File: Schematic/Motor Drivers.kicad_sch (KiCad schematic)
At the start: 16 parts, among them U18 DRV8243SQDGQRQ1 (S-Variant), U19 DRV8243SQDGQRQ1 (S-Variant)

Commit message: 100n cap
100n cap bom
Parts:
- C71, C72: footprint (none) -> CL10B104MB8NNNC:CAPC1608X90N; Link (none) -> https://mou.sr/3JWJm45; Manufacturer Part Number (none) -> CL10B104MB8NNNC; Price per Unit (none) -> 0.10; Supplier (none) -> Mouser; Supplier Part Number (none) -> 187-CL10B104MB8NNNC
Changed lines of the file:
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@@
 			)
 		)
-		(property "Footprint" ""
+		(property "Footprint" "CL10B104MB8NNNC:CAPC1608X90N"
 			(at 69.5452 59.69 0)
 			(effects
@@
 			)
 		)
-		(property "Link" ""
+		(property "Link" "https://mou.sr/3JWJm45"
 			(at 68.58 55.88 0)
 			(effects
@@
 			)
 		)
-		(property "Manufacturer Part Number" ""
+		(property "Manufacturer Part Number" "CL10B104MB8NNNC"
 			(at 68.58 55.88 0)
 			(effects
@@
 			)
 		)
-		(property "Price per Unit" ""
+		(property "Price per Unit" "0.10"
 			(at 68.58 55.88 0)
 			(effects
@@
 			)
 		)
-		(property "Supplier" ""
+		(property "Supplier" "Mouser"
 			(at 68.58 55.88 0)
 			(effects
@@
 			)
 		)
-		(property "Supplier Part Number" ""
+		(property "Supplier Part Number" "187-CL10B104MB8NNNC "
 			(at 68.58 55.88 0)
 			(effects
@@
 			)
 		)
-		(property "Footprint" ""
+		(property "Footprint" "CL10B104MB8NNNC:CAPC1608X90N"
 			(at 67.0052 128.27 0)
 			(effects
@@
 			)
 		)
-		(property "Link" ""
+		(property "Link" "https://mou.sr/3JWJm45"
 			(at 66.04 124.46 0)
 			(effects
@@
 			)
 		)
-		(property "Manufacturer Part Number" ""
+		(property "Manufacturer Part Number" "CL10B104MB8NNNC"
 			(at 66.04 124.46 0)
 			(effects
@@
 			)
 		)
-		(property "Price per Unit" ""
+		(property "Price per Unit" "0.10"
 			(at 66.04 124.46 0)
 			(effects
@@
 			)
 		)
-		(property "Supplier" ""
+		(property "Supplier" "Mouser"
 			(at 66.04 124.46 0)
 			(effects
@@
 			)
 		)
-		(property "Supplier Part Number" ""
+		(property "Supplier Part Number" "187-CL10B104MB8NNNC "
 			(at 66.04 124.46 0)
 			(effects

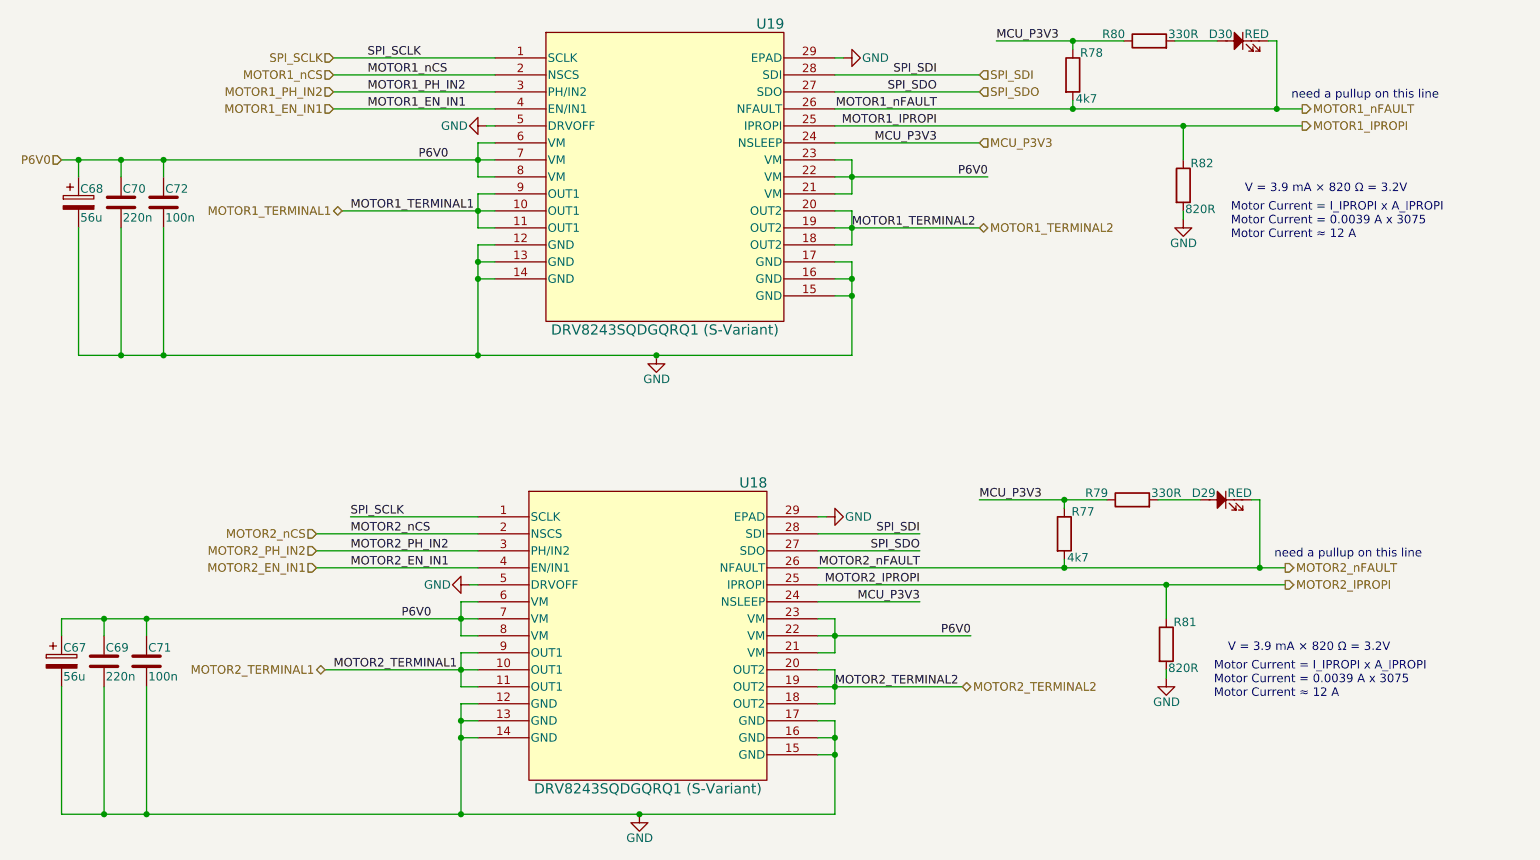
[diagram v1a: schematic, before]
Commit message: added test points and fet
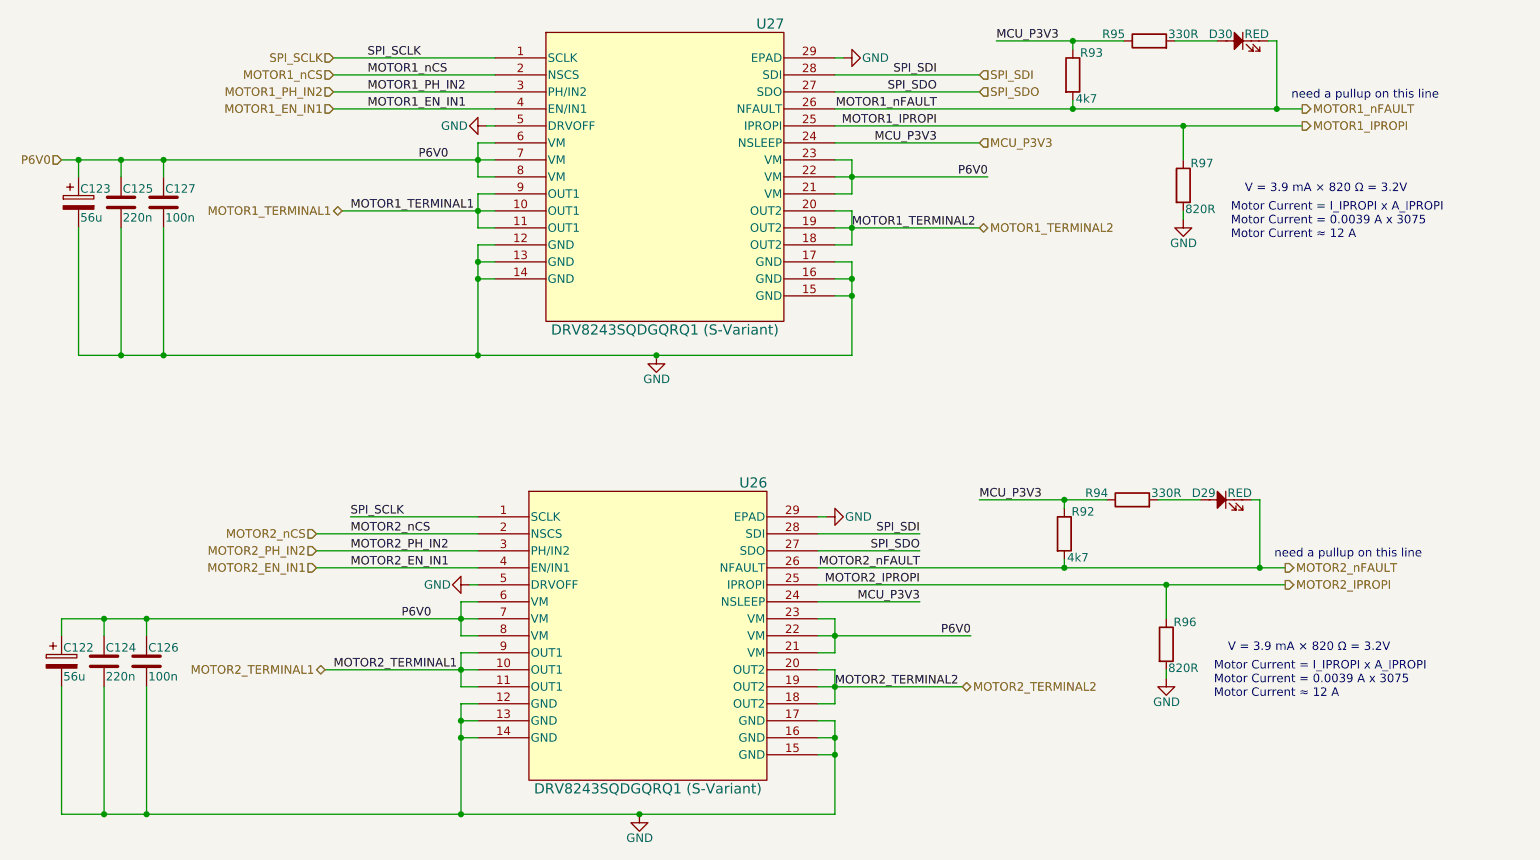
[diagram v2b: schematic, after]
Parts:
- C126: renamed from C71; footprint CL10B104MB8NNNC:CAPC1608X90N -> Capacitor_SMD:C_0603_1608Metric_Pad1.08x0.95mm_HandSolder
- C127: renamed from C72; footprint CL10B104MB8NNNC:CAPC1608X90N -> Capacitor_SMD:C_0603_1608Metric_Pad1.08x0.95mm_HandSolder
- renumbered C67 to C122, C68 to C123, C69 to C124, C70 to C125, R77 to R92, R78 to R93, R79 to R94, R80 to R95, R81 to R96, R82 to R97, U18 to U26, U19 to U27
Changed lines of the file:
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@@
 		(on_board yes)
 		(dnp no)
-		(property "Reference" "C72"
+		(property "Reference" "C127"
 			(at 68.834 53.848 0)
 			(effects
@@
 			)
 		)
-		(property "Footprint" "CL10B104MB8NNNC:CAPC1608X90N"
+		(property "Footprint" "Capacitor_SMD:C_0603_1608Metric_Pad1.08x0.95mm_HandSolder"
 			(at 69.5452 59.69 0)
 			(effects
@@
 			(project "STAR"
 				(path "/fc8533bc-25dd-4c20-9b4c-ffebebd6739b/f73d6367-f3ba-42df-a3ea-bd155f1c219f/07712c52-f5ae-4a00-8c08-8de30640eab9"
-					(reference "C72")
+					(reference "C127")
 					(unit 1)
 				)
@@
 		(on_board yes)
 		(dnp no)
-		(property "Reference" "R79"
+		(property "Reference" "R94"
 			(at 208.026 99.314 90)
 			(effects
@@
 			(project "STAR"
 				(path "/fc8533bc-25dd-4c20-9b4c-ffebebd6739b/f73d6367-f3ba-42df-a3ea-bd155f1c219f/07712c52-f5ae-4a00-8c08-8de30640eab9"
-					(reference "R79")
+					(reference "R94")
 					(unit 1)
 				)
@@
 		(on_board yes)
 		(dnp no)
-		(property "Reference" "#PWR043"
+		(property "Reference" "#PWR068"
 			(at 110.49 44.45 0)
 			(effects
@@
 			(project "STAR"
 				(path "/fc8533bc-25dd-4c20-9b4c-ffebebd6739b/f73d6367-f3ba-42df-a3ea-bd155f1c219f/07712c52-f5ae-4a00-8c08-8de30640eab9"
-					(reference "#PWR043")
+					(reference "#PWR068")
 					(unit 1)
 				)
@@
 		(on_board yes)
 		(dnp no)
-		(property "Reference" "#PWR046"
+		(property "Reference" "#PWR071"
 			(at 173.99 102.87 0)
 			(effects
@@
 			(project "STAR"
 				(path "/fc8533bc-25dd-4c20-9b4c-ffebebd6739b/f73d6367-f3ba-42df-a3ea-bd155f1c219f/07712c52-f5ae-4a00-8c08-8de30640eab9"
-					(reference "#PWR046")
+					(reference "#PWR071")
 					(unit 1)
 				)
@@
 		(on_board yes)
 		(dnp no)
-		(property "Reference" "R80"
+		(property "Reference" "R95"
 			(at 210.566 30.734 90)
 			(effects
@@
 			(project "STAR"
 				(path "/fc8533bc-25dd-4c20-9b4c-ffebebd6739b/f73d6367-f3ba-42df-a3ea-bd155f1c219f/07712c52-f5ae-4a00-8c08-8de30640eab9"
-					(reference "R80")
+					(reference "R95")
 					(unit 1)
 				)
@@
 		(on_board yes)
 		(dnp no)
-		(property "Reference" "#PWR047"
+		(property "Reference" "#PWR072"
 			(at 176.53 34.29 0)
 			(effects
@@
 			(project "STAR"
 				(path "/fc8533bc-25dd-4c20-9b4c-ffebebd6739b/f73d6367-f3ba-42df-a3ea-bd155f1c219f/07712c52-f5ae-4a00-8c08-8de30640eab9"
-					(reference "#PWR047")
+					(reference "#PWR072")
 					(unit 1)
 				)
@@
 		(on_board yes)
 		(dnp no)
-		(property "Reference" "C70"
+		(property "Reference" "C125"
 			(at 62.484 53.848 0)
 			(effects
@@
 			(project "STAR"
 				(path "/fc8533bc-25dd-4c20-9b4c-ffebebd6739b/f73d6367-f3ba-42df-a3ea-bd155f1c219f/07712c52-f5ae-4a00-8c08-8de30640eab9"
-					(reference "C70")
+					(reference "C125")
 					(unit 1)
 				)
@@
 		(on_board yes)
 		(dnp no)
-		(property "Reference" "C68"
+		(property "Reference" "C123"
 			(at 56.134 53.848 0)
 			(effects
@@
 			(project "STAR"
 				(path "/fc8533bc-25dd-4c20-9b4c-ffebebd6739b/f73d6367-f3ba-42df-a3ea-bd155f1c219f/07712c52-f5ae-4a00-8c08-8de30640eab9"
-					(reference "C68")
+					(reference "C123")
 					(unit 1)
 				)
@@
 		(on_board yes)
 		(dnp no)
-		(property "Reference" "U19"
+		(property "Reference" "U27"
 			(at 159.258 29.21 0)
 			(effects
@@
 			(project "STAR"
 				(path "/fc8533bc-25dd-4c20-9b4c-ffebebd6739b/f73d6367-f3ba-42df-a3ea-bd155f1c219f/07712c52-f5ae-4a00-8c08-8de30640eab9"
-					(reference "U19")
+					(reference "U27")
 					(unit 1)
 				)
@@
 		(on_board yes)
 		(dnp no)
-		(property "Reference" "C67"
+		(property "Reference" "C122"
 			(at 53.594 122.428 0)
 			(effects
@@
 			(project "STAR"
 				(path "/fc8533bc-25dd-4c20-9b4c-ffebebd6739b/f73d6367-f3ba-42df-a3ea-bd155f1c219f/07712c52-f5ae-4a00-8c08-8de30640eab9"
-					(reference "C67")
+					(reference "C122")
 					(unit 1)
 				)
@@
 		(on_board yes)
 		(dnp no)
-		(property "Reference" "U18"
+		(property "Reference" "U26"
 			(at 156.718 97.79 0)
 			(effects
@@
 			(project "STAR"
 				(path "/fc8533bc-25dd-4c20-9b4c-ffebebd6739b/f73d6367-f3ba-42df-a3ea-bd155f1c219f/07712c52-f5ae-4a00-8c08-8de30640eab9"
-					(reference "U18")
+					(reference "U26")
 					(unit 1)
 				)
@@
 		(on_board yes)
 		(dnp no)
-		(property "Reference" "R82"
+		(property "Reference" "R97"
 			(at 223.774 50.038 0)
 			(effects
@@
 			(project "STAR"
 				(path "/fc8533bc-25dd-4c20-9b4c-ffebebd6739b/f73d6367-f3ba-42df-a3ea-bd155f1c219f/07712c52-f5ae-4a00-8c08-8de30640eab9"
-					(reference "R82")
+					(reference "R97")
 					(unit 1)
 				)
@@
 		(on_board yes)
 		(dnp no)
-		(property "Reference" "R77"
+		(property "Reference" "R92"
 			(at 205.994 102.108 0)
 			(effects
@@
 			(project "STAR"
 				(path "/fc8533bc-25dd-4c20-9b4c-ffebebd6739b/f73d6367-f3ba-42df-a3ea-bd155f1c219f/07712c52-f5ae-4a00-8c08-8de30640eab9"
-					(reference "R77")
+					(reference "R92")
 					(unit 1)
 				)
@@
 		(on_board yes)
 		(dnp no)
-		(property "Reference" "#PWR044"
+		(property "Reference" "#PWR069"
 			(at 139.7 153.67 0)
 			(effects
@@
 			(project "STAR"
 				(path "/fc8533bc-25dd-4c20-9b4c-ffebebd6739b/f73d6367-f3ba-42df-a3ea-bd155f1c219f/07712c52-f5ae-4a00-8c08-8de30640eab9"
-					(reference "#PWR044")
+					(reference "#PWR069")
 					(unit 1)
 				)
@@
 		(on_board yes)
 		(dnp no)
-		(property "Reference" "C71"
+		(property "Reference" "C126"
 			(at 66.294 122.428 0)
 			(effects
@@
 			)
 		)
-		(property "Footprint" "CL10B104MB8NNNC:CAPC1608X90N"
+		(property "Footprint" "Capacitor_SMD:C_0603_1608Metric_Pad1.08x0.95mm_HandSolder"
 			(at 67.0052 128.27 0)
 			(effects
@@
 			(project "STAR"
 				(path "/fc8533bc-25dd-4c20-9b4c-ffebebd6739b/f73d6367-f3ba-42df-a3ea-bd155f1c219f/07712c52-f5ae-4a00-8c08-8de30640eab9"
-					(reference "C71")
+					(reference "C126")
 					(unit 1)
 				)
@@
 		(on_board yes)
 		(dnp no)
-		(property "Reference" "#PWR049"
+		(property "Reference" "#PWR074"
 			(at 220.98 64.77 0)
 			(effects
@@
 			(project "STAR"
 				(path "/fc8533bc-25dd-4c20-9b4c-ffebebd6739b/f73d6367-f3ba-42df-a3ea-bd155f1c219f/07712c52-f5ae-4a00-8c08-8de30640eab9"
-					(reference "#PWR049")
+					(reference "#PWR074")
 					(unit 1)
 				)
@@
 		(on_board yes)
 		(dnp no)
-		(property "Reference" "#PWR042"
+		(property "Reference" "#PWR067"
 			(at 107.95 113.03 0)
 			(effects
@@
 			(project "STAR"
 				(path "/fc8533bc-25dd-4c20-9b4c-ffebebd6739b/f73d6367-f3ba-42df-a3ea-bd155f1c219f/07712c52-f5ae-4a00-8c08-8de30640eab9"
-					(reference "#PWR042")
+					(reference "#PWR067")
 					(unit 1)
 				)
@@
 		(on_board yes)
 		(dnp no)
-		(property "Reference" "C69"
+		(property "Reference" "C124"
 			(at 59.944 122.428 0)
 			(effects
@@
 			(project "STAR"
 				(path "/fc8533bc-25dd-4c20-9b4c-ffebebd6739b/f73d6367-f3ba-42df-a3ea-bd155f1c219f/07712c52-f5ae-4a00-8c08-8de30640eab9"
-					(reference "C69")
+					(reference "C124")
 					(unit 1)
 				)
@@
 		(on_board yes)
 		(dnp no)
-		(property "Reference" "#PWR048"
+		(property "Reference" "#PWR073"
 			(at 218.44 133.35 0)
 			(effects
@@
 			(project "STAR"
 				(path "/fc8533bc-25dd-4c20-9b4c-ffebebd6739b/f73d6367-f3ba-42df-a3ea-bd155f1c219f/07712c52-f5ae-4a00-8c08-8de30640eab9"
-					(reference "#PWR048")
+					(reference "#PWR073")
 					(unit 1)
 				)
@@
 		(on_board yes)
 		(dnp no)
-		(property "Reference" "R81"
+		(property "Reference" "R96"
 			(at 221.234 118.618 0)
 			(effects
@@
 			(project "STAR"
 				(path "/fc8533bc-25dd-4c20-9b4c-ffebebd6739b/f73d6367-f3ba-42df-a3ea-bd155f1c219f/07712c52-f5ae-4a00-8c08-8de30640eab9"
-					(reference "R81")
+					(reference "R96")
 					(unit 1)
 				)
@@
 		(on_board yes)
 		(dnp no)
-		(property "Reference" "R78"
+		(property "Reference" "R93"
 			(at 207.264 33.528 0)
 			(effects
@@
 			(project "STAR"
 				(path "/fc8533bc-25dd-4c20-9b4c-ffebebd6739b/f73d6367-f3ba-42df-a3ea-bd155f1c219f/07712c52-f5ae-4a00-8c08-8de30640eab9"
-					(reference "R78")
+					(reference "R93")
 					(unit 1)
 				)
@@
 		(on_board yes)
 		(dnp no)
-		(property "Reference" "#PWR045"
+		(property "Reference" "#PWR070"
 			(at 142.24 85.09 0)
 			(effects
@@
 			(project "STAR"
 				(path "/fc8533bc-25dd-4c20-9b4c-ffebebd6739b/f73d6367-f3ba-42df-a3ea-bd155f1c219f/07712c52-f5ae-4a00-8c08-8de30640eab9"
-					(reference "#PWR045")
+					(reference "#PWR070")
 					(unit 1)
 				)

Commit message: More REsistor
16 res down for bom
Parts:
- R92, R93: footprint (none) -> Resistor_SMD:R_0603_1608Metric_Pad0.98x0.95mm_HandSolder; Link (none) -> https://mou.sr/48a41vp; Manufacturer Part Number (none) -> RCS06034K70FKEA; Price per Unit (none) -> 0.13; Supplier (none) -> Mouser; Supplier Part Number (none) -> 71-RCS06034K70FKEA
- R95: footprint (none) -> Resistor_SMD:R_0603_1608Metric_Pad0.98x0.95mm_HandSolder; Link (none) -> https://mou.sr/4m95jdp; Manufacturer Part Number (none) -> RG1608P-331-D-T5; Price per Unit (none) -> 0.10; Supplier (none) -> Mouser; Supplier Part Number (none) -> 754-RG1608P-331DT5
- R96: footprint (none) -> Resistor_SMD:R_0603_1608Metric_Pad0.98x0.95mm_HandSolder; Link (none) -> https://mou.sr/46iPyuQ; Manufacturer Part Number (none) -> RMC1/16K8200FTP; Price per Unit (none) -> 0.10; Supplier (none) -> Mouser; Supplier Part Number (none) -> 791-RMC1/16K8200FTP
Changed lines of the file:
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@@
 			)
 		)
-		(property "Footprint" ""
+		(property "Footprint" "Resistor_SMD:R_0603_1608Metric_Pad0.98x0.95mm_HandSolder"
 			(at 215.9 33.528 90)
 			(effects
@@
 			)
 		)
-		(property "Link" ""
+		(property "Link" "https://mou.sr/4m95jdp"
 			(at 215.9 31.75 90)
 			(effects
@@
 			)
 		)
-		(property "Manufacturer Part Number" ""
+		(property "Manufacturer Part Number" "RG1608P-331-D-T5 "
 			(at 215.9 31.75 90)
 			(effects
@@
 			)
 		)
-		(property "Price per Unit" ""
+		(property "Price per Unit" "0.10"
 			(at 215.9 31.75 90)
 			(effects
@@
 			)
 		)
+		(property "Supplier" "Mouser"
+			(at 215.9 31.75 90)
+			(effects
+				(font
+					(size 1.27 1.27)
+				)
+				(hide yes)
+			)
+		)
+		(property "Supplier Part Number" "754-RG1608P-331DT5"
+			(at 215.9 31.75 90)
+			(effects
+				(font
+					(size 1.27 1.27)
+				)
+				(hide yes)
+			)
+		)
 		(pin "1"
 		)
@@
 			)
 		)
-		(property "Footprint" ""
+		(property "Footprint" "Resistor_SMD:R_0603_1608Metric_Pad0.98x0.95mm_HandSolder"
 			(at 201.422 105.41 90)
 			(effects
@@
 			)
 		)
-		(property "Link" ""
+		(property "Link" "https://mou.sr/48a41vp"
 			(at 203.2 105.41 0)
 			(effects
@@
 			)
 		)
-		(property "Manufacturer Part Number" ""
+		(property "Manufacturer Part Number" "RCS06034K70FKEA "
 			(at 203.2 105.41 0)
 			(effects
@@
 			)
 		)
-		(property "Price per Unit" ""
+		(property "Price per Unit" "0.13"
 			(at 203.2 105.41 0)
 			(effects
@@
 			)
 		)
+		(property "Supplier" "Mouser"
+			(at 203.2 105.41 0)
+			(effects
+				(font
+					(size 1.27 1.27)
+				)
+				(hide yes)
+			)
+		)
+		(property "Supplier Part Number" "71-RCS06034K70FKEA "
+			(at 203.2 105.41 0)
+			(effects
+				(font
+					(size 1.27 1.27)
+				)
+				(hide yes)
+			)
+		)
 		(pin "1"
 		)
@@
 			)
 		)
-		(property "Footprint" ""
+		(property "Footprint" "Resistor_SMD:R_0603_1608Metric_Pad0.98x0.95mm_HandSolder"
 			(at 216.662 121.92 90)
 			(effects
@@
 			)
 		)
-		(property "Link" ""
+		(property "Link" "https://mou.sr/46iPyuQ"
 			(at 218.44 121.92 0)
 			(effects
@@
 			)
 		)
-		(property "Manufacturer Part Number" ""
+		(property "Manufacturer Part Number" "RMC1/16K8200FTP "
 			(at 218.44 121.92 0)
 			(effects
@@
 			)
 		)
-		(property "Price per Unit" ""
+		(property "Price per Unit" "0.10"
 			(at 218.44 121.92 0)
 			(effects
@@
 			)
 		)
+		(property "Supplier" "Mouser"
+			(at 218.44 121.92 0)
+			(effects
+				(font
+					(size 1.27 1.27)
+				)
+				(hide yes)
+			)
+		)
+		(property "Supplier Part Number" "791-RMC1/16K8200FTP "
+			(at 218.44 121.92 0)
+			(effects
+				(font
+					(size 1.27 1.27)
+				)
+				(hide yes)
+			)
+		)
 		(pin "1"
 		)
@@
 			)
 		)
-		(property "Footprint" ""
+		(property "Footprint" "Resistor_SMD:R_0603_1608Metric_Pad0.98x0.95mm_HandSolder"
 			(at 202.692 36.83 90)
 			(effects
@@
 			)
 		)
-		(property "Link" ""
+		(property "Link" "https://mou.sr/48a41vp"
 			(at 204.47 36.83 0)
 			(effects
@@
 			)
 		)
-		(property "Manufacturer Part Number" ""
+		(property "Manufacturer Part Number" "RCS06034K70FKEA "
 			(at 204.47 36.83 0)
 			(effects
@@
 			)
 		)
-		(property "Price per Unit" ""
+		(property "Price per Unit" "0.13"
 			(at 204.47 36.83 0)
 			(effects
@@
 			(at 204.47 36.83 0)
 			(effects
+				(font
+					(size 1.27 1.27)
+				)
+				(hide yes)
+			)
+		)
+		(property "Supplier" "Mouser"
+			(at 204.47 36.83 0)
+			(effects
+				(font
+					(size 1.27 1.27)
+				)
+				(hide yes)
+			)
+		)
+		(property "Supplier Part Number" "71-RCS06034K70FKEA "
+			(at 204.47 36.83 0)
+			(effects
